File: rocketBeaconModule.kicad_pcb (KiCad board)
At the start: 2 copper layers, 80.5 x 49.3 mm, 72 parts, among them J1 Main Bus, J2 Jumper Select, J3 TYPE-C-31-M-12, P1 AntMount, U1 STM32F401CCU6, U2 AMS1117-3.3, U3 CC1200, X1 40mhz, Y1 16MHz

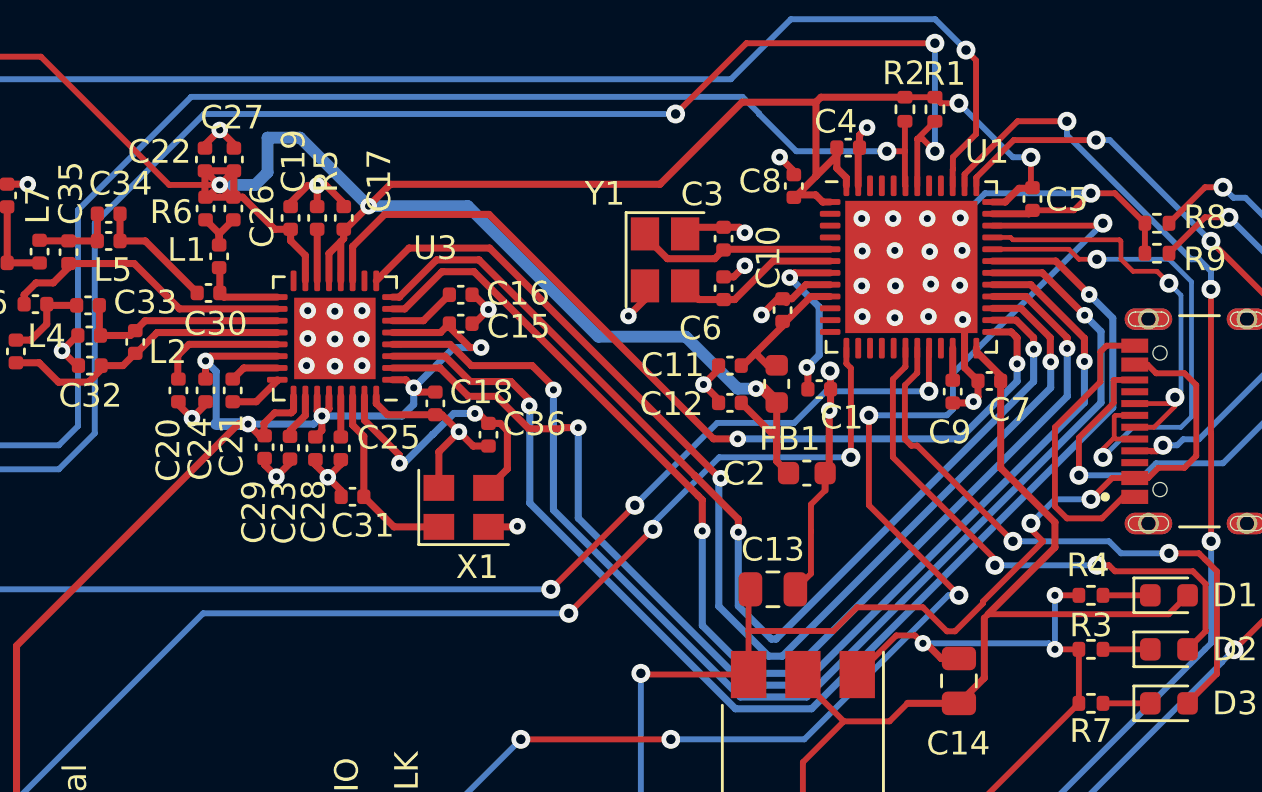
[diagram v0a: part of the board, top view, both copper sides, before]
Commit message: fixed usb / io footprint mixup
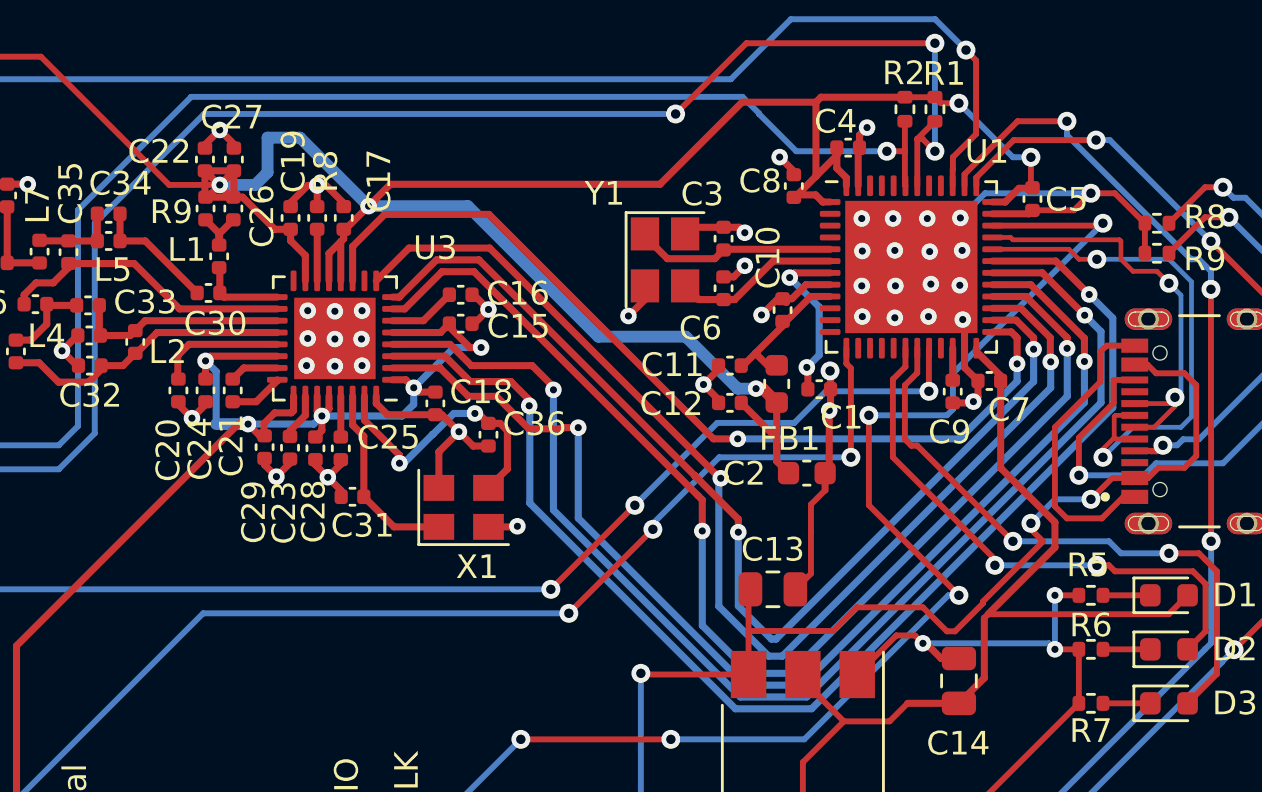
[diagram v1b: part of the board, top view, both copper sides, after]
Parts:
- renumbered J3 to J1, J1 to J3, R4 to R5, R3 to R6, R5 to R8, R6 to R9

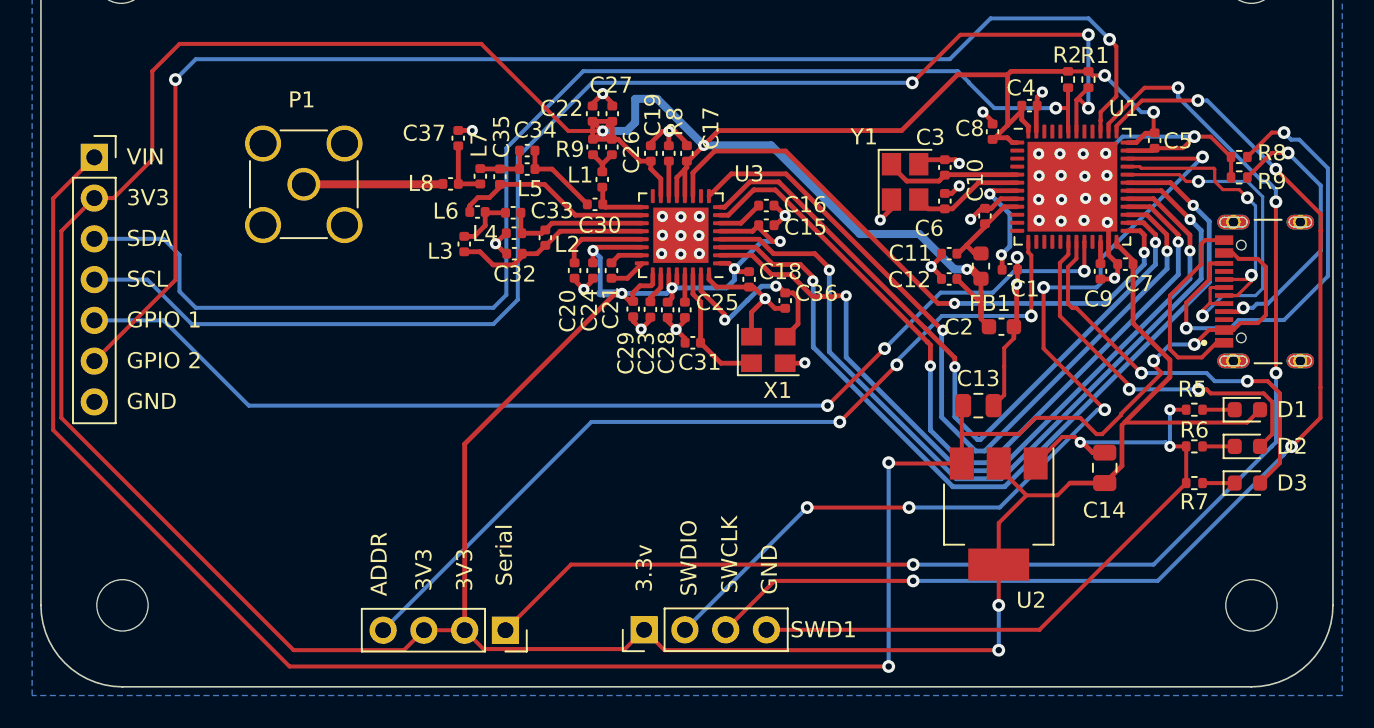
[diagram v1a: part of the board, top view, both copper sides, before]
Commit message: removed old footprints and replaced with new ones
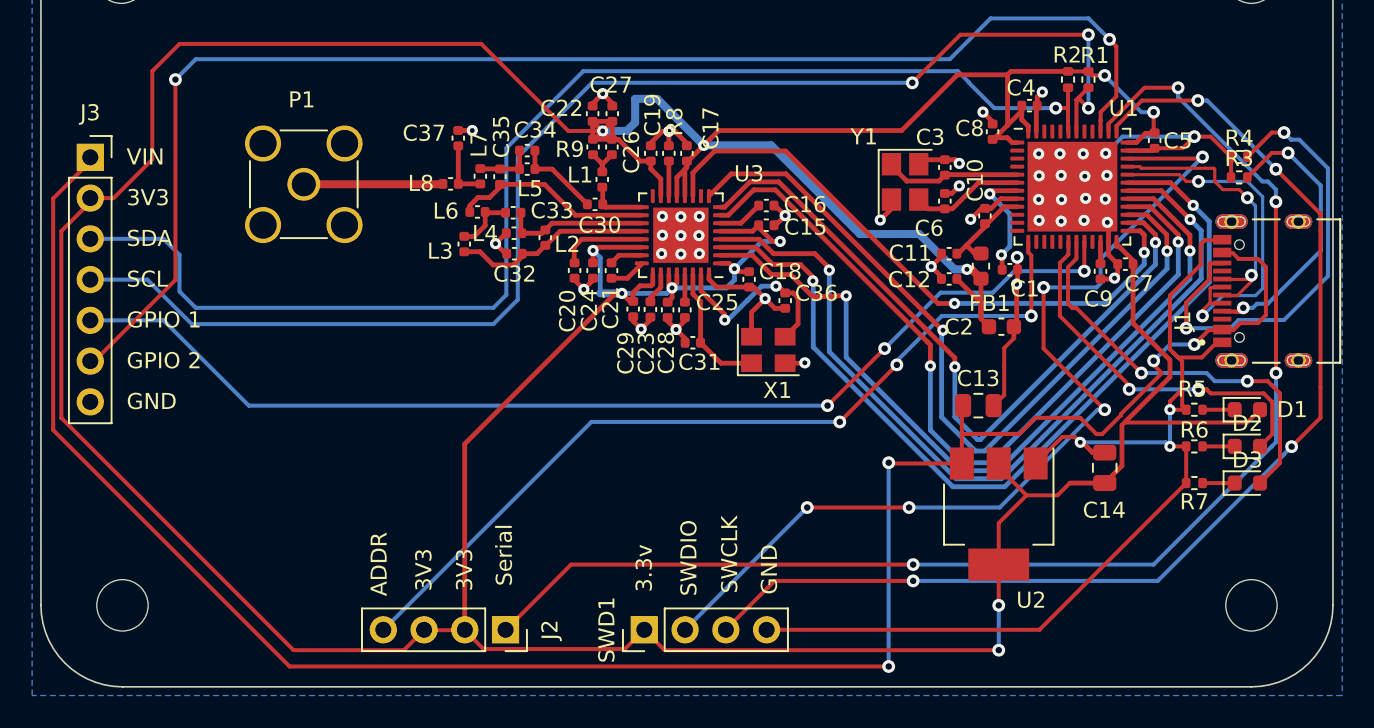
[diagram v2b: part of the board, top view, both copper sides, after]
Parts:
- removed the R8 at (224.5, 82.5)
- removed the R9 at (224.5, 83.8)
- added R3: 5.11k, Resistor_SMD:R_0402_1005Metric, F.Cu at (224.5, 83.8)
- added R4: 5.11k, Resistor_SMD:R_0402_1005Metric, F.Cu at (224.5, 82.5)
- moved J3 0.25 mm to (152.9, 82.6)
- moved J1 0.12 mm to (228.2, 90.9)
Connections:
- J1 pad A1/B12: Net-(J3-PadA1/B12) -> GND
- J1 pad B1/A12: Net-(J3-PadA1/B12) -> GND
- J1 pad S1: unconnected-(J3-PadS1) -> unconnected-(J1-PadS1)
- J1 pad S2: unconnected-(J3-PadS1) -> unconnected-(J1-PadS2)
- J1 pad S3: unconnected-(J3-PadS1) -> unconnected-(J1-PadS3)
- J1 pad S4: unconnected-(J3-PadS1) -> unconnected-(J1-PadS4)
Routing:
- net GND: track 118.5 -> 136.8 mm
- net Net-(J3-PadA1/B12): track 12.9 -> 0.00 mm

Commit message: DRC resolution on PCB layouts
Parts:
- moved J1 0.13 mm to (228.4, 90.9)
